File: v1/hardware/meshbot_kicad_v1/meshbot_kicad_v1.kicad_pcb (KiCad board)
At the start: 2 copper layers, 51.9 x 23.2 mm, 9 parts, among them J1 Conn_01x02_Socket, J2 Conn_01x04_Pin, J3 Conn_01x04_Pin, J4 Conn_01x01_Socket, SW1 SW_Push, U1 wio-sx1262, U2 nice_nano_clean

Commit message: update
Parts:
- added D2: LED, LED_THT:LED_D5.0mm, F.Cu at (29.4, 1.60)
- added H1: MountingHole, MountingHole:MountingHole_3.2mm_M3, F.Cu at (0.00, 0.00)
- added H2: MountingHole, MountingHole:MountingHole_3.2mm_M3, F.Cu at (81.0, 0.00)
- added H3: MountingHole, MountingHole:MountingHole_3.2mm_M3, F.Cu at (81.0, 66.0)
- added H4: MountingHole, MountingHole:MountingHole_3.2mm_M3, F.Cu at (0.10, 66.0)
- added J11: Conn_01x03_Pin, Connector_PinHeader_2.54mm:PinHeader_1x03_P2.54mm_Vertical, F.Cu at (24.3, 57.4)
- added J12: Conn_01x03_Pin, Connector_PinHeader_2.54mm:PinHeader_1x03_P2.54mm_Vertical, F.Cu at (24.2, 64.3)
- added J13: Conn_01x08_Socket, Connector_PinSocket_2.54mm:PinSocket_1x08_P2.54mm_Vertical, F.Cu at (5.62, 1.38)
- added J5: Conn_01x04_Pin, footprints:ssd1306_a, F.Cu at (63.0, 28.1)
- added J6: Screw_Terminal_01x04, TerminalBlock_Phoenix:TerminalBlock_Phoenix_MKDS-1,5-4-5.08_1x04_P5.08mm_Horizontal, F.Cu at (45.7, 62.3)
- added J7: Screw_Terminal_01x03, TerminalBlock_Phoenix:TerminalBlock_Phoenix_MKDS-1,5-3-5.08_1x03_P5.08mm_Horizontal, F.Cu at (29.4, 62.3)
- added J8: Conn_01x03_Socket, footprints:usual_switch, F.Cu at (73.2, 1.70)
- added J9: Conn_01x02_Socket, Buzzer_Beeper:Buzzer_12x9.5RM7.6, F.Cu at (36.8, 19.7)
- added R3: R, Resistor_THT:R_Axial_DIN0204_L3.6mm_D1.6mm_P1.90mm_Vertical, F.Cu at (24.8, 4.30)
- added R4: R, Resistor_THT:R_Axial_DIN0204_L3.6mm_D1.6mm_P1.90mm_Vertical, F.Cu at (18.2, 4.30)
- added R5: R, Resistor_THT:R_Axial_DIN0204_L3.6mm_D1.6mm_P1.90mm_Vertical, F.Cu at (54.0, 3.00)
- added R6: R, Resistor_THT:R_Axial_DIN0204_L3.6mm_D1.6mm_P1.90mm_Vertical, F.Cu at (51.5, 3.00)
- added R7: R, Resistor_THT:R_Axial_DIN0204_L3.6mm_D1.6mm_P1.90mm_Vertical, F.Cu at (49.0, 3.00)
- added SW2: SW_Push, Button_Switch_THT:SW_Tactile_SPST_Angled_PTS645Vx31-2LFS, F.Cu at (-0.10, 40.6)
- added SW3: SW_Push, Button_Switch_THT:SW_Tactile_SPST_Angled_PTS645Vx31-2LFS, F.Cu at (81.5, 26.5)
- added SW4: SW_Push, Button_Switch_THT:SW_Tactile_SPST_Angled_PTS645Vx31-2LFS, F.Cu at (81.5, 36.1)
- added SW5: SW_Push, Button_Switch_THT:SW_Tactile_SPST_Angled_PTS645Vx31-2LFS, F.Cu at (81.5, 45.7)
- added SW6: SW_Push, Button_Switch_THT:SW_Tactile_SPST_Angled_PTS645Vx31-2LFS, F.Cu at (81.5, 55.4)
- added SW7: SW_Push, Button_Switch_THT:SW_Tactile_SPST_Angled_PTS645Vx31-2LFS, F.Cu at (-0.10, 50.2)
- added SW8: SW_Push, Button_Switch_THT:SW_Tactile_SPST_Angled_PTS645Vx31-2LFS, F.Cu at (-0.10, 59.8)
- added U3: nice_nano_clean, footprints:nice_nano_cleanest, F.Cu at (65.5, 14.6)
- added U4: grove_a, footprints:grove_a, F.Cu at (14.5, 59.9)
- added U5: grove_a, footprints:grove_rightangle, F.Cu at (73.1, 60.0)
- J2: footprint Connector_PinHeader_2.54mm:PinHeader_1x04_P2.54mm_Vertical -> footprints:gps_ublox_blue
- J3: footprint Connector_PinHeader_2.54mm:PinHeader_1x04_P2.54mm_Vertical -> footprints:ssd1306_a
- SW1: footprint Button_Switch_THT:SW_PUSH_6mm -> Button_Switch_THT:SW_Tactile_SPST_Angled_PTS645Vx31-2LFS
- moved SW1 96.7 mm to (-0.10, 31.0)
- moved J4 79.4 mm to (41.4, -1.20)
- moved U2 66.1 mm to (15.7, 14.7)
- moved U1 64.6 mm to (34.8, 12.2), turned to 0 degrees
- moved R2 60.4 mm to (5.60, 4.30), turned to 180 degrees
- moved R1 59.8 mm to (11.7, 4.30), turned to 180 degrees
- moved J3 58.5 mm to (26.1, 28.1), turned to -90 degrees
- moved J1 52.8 mm to (60.8, 2.40), turned to 180 degrees
- moved J2 45.4 mm to (37.0, 37.8), turned to -90 degrees
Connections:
- net BATT_MEASURE renamed MESH_BATT_MEASURE
- net MICRO_RST renamed MESH_RST
- net SCL renamed SCL_MESH
- net SDA renamed SDA_MESH
- J1 pad 1: BAT -> V_EXT
- J3 pad 1: GND -> 3V3
- J3 pad 2: 3V3 -> GND
- U2 pad 1: unconnected-(U2-TX0/P0.06-Pad1) -> MESH_TX
- U2 pad 12: unconnected-(U2-P1.06-Pad12) -> MESH_BUTTON_C
- U2 pad 2: unconnected-(U2-RX1/P0.08-Pad2) -> MESH_RX
- U2 pad 8: unconnected-(U2-P0.24-Pad8) -> MESH_BUTTON_A
- U2 pad 9: unconnected-(U2-P1.00-Pad9) -> MESH_BUTTON_B
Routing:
- net GND: track 111.4 -> 0.00 mm, vias 11 -> 0
- net GPS_TX: track 70.5 -> 0.00 mm, vias 4 -> 0
- net 3V3: track 62.9 -> 0.00 mm, vias 5 -> 0
- net GPS_RX: track 60.5 -> 0.00 mm, vias 5 -> 0
- net BAT: track 59.6 -> 0.00 mm, vias 3 -> 0
- net BUSY: track 37.5 -> 0.00 mm, vias 4 -> 0
- net SDA_MESH: track 36.6 -> 0.00 mm, vias 3 -> 0
- net MESH_RST: track 36.5 -> 0.00 mm, vias 1 -> 0
- net RF_SW: track 32.5 -> 0.00 mm, vias 2 -> 0
- net SCL_MESH: track 31.4 -> 0.00 mm, vias 3 -> 0
- net MOSI: track 24.0 -> 0.00 mm, vias 2 -> 0
- net MISO: track 23.5 -> 0.00 mm, vias 2 -> 0
- net DIO1: track 23.1 -> 0.00 mm, vias 4 -> 0
- net CS: track 22.8 -> 0.00 mm, vias 2 -> 0
- net SCK: track 18.3 -> 0.00 mm, vias 2 -> 0
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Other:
- board size 51.9 x 23.2 mm -> 88 x 72.7 mm
- board text added: "+"
- board text added: "-"
- board text added: "1W"
- board text added: "2"
- board text added: "29"
- board text added: "3V3"
- board text added: "A"
- board text added: "ANT"
- board text added: "B"
- board text added: "Buzzer"
- board text added: "C"
- board text added: "GPS_RX"
- board text added: "GPS_TX"
- board text added: "M:A"
- board text added: "M:B"
- board text added: "M:C"
- board text added: "M:RST"
- board text added: "M:SCL"
- board text added: "M:SDA"
- board text added: "MESHBOT VER 1"
- board text added: "OFF"
- board text added: "ON"
- board text added: "RX"
- board text added: "SSD1306"
- board text added: "S_A"
- board text added: "S_B"
- board text added: "TX"
- board text added: "VEX"
- board text added: "edgecollective.io/meshbot"
- board text added: "v1"
- board text removed: "20"
- board text removed: "22"
- board text removed: "ANTENNA"
- board text removed: "v0.2"
- board text removed: "waterbearfieldschool.org/thistle"

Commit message: update
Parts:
- D2: footprint LED_THT:LED_D5.0mm -> LED_THT:LED_D3.0mm
- moved J8 59.1 mm to (14.1, -0.10)
- moved J13 52.0 mm to (57.6, 2.27)
- moved J1 35.3 mm to (25.6, 0.40)
- moved D2 3.10 mm to (32.3, 0.50)
- moved R2 2.01 mm to (3.60, 4.20), turned to 0 degrees
- moved R1 2.01 mm to (9.70, 4.20), turned to 0 degrees
- moved R3 0.41 mm to (24.4, 4.20)
- moved R4 0.32 mm to (17.9, 4.20)
- moved J12 0.20 mm to (24.2, 64.5)
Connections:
- J13 pad 4: GND -> SDA
- J13 pad 6: SDA -> P0.2
- J13 pad 7: P0.2 -> P0.29
- J13 pad 8: P0.29 -> GND
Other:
- board text added: "NEO6M GPS"
- board text added: "S:A"
- board text added: "S:B"
- board text added: "VEXT"
- board text removed: "S_A"
- board text removed: "S_B"
- board text removed: "VEX"

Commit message: update
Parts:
- moved H1 112.7 mm to (104.4, 42.5)
- moved H2 112.7 mm to (185.4, 42.5)
- moved H3 112.7 mm to (185.4, 108.5)
- moved H4 112.7 mm to (104.5, 108.5)
- moved J1 112.7 mm to (130.0, 42.9)
- moved J11 112.7 mm to (128.7, 99.9)
- moved J12 112.7 mm to (128.6, 107.0)
- moved J13 112.7 mm to (162.0, 44.8)
- moved J2 112.7 mm to (141.4, 80.3)
- moved J3 112.7 mm to (130.5, 70.6)
- moved J4 112.7 mm to (145.8, 41.3)
- moved J7 112.7 mm to (133.8, 104.8)
- moved J8 112.7 mm to (118.5, 42.4)
- moved R1 112.7 mm to (114.1, 46.7)
- moved R2 112.7 mm to (108.0, 46.7)
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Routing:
- net BAT: track 0.00 -> 143.1 mm, vias 0 -> 13
- net GND: track 0.00 -> 74.3 mm, vias 0 -> 12
- net V_EXT: track 0.00 -> 54.9 mm, vias 0 -> 3
- net 3V3: track 0.00 -> 42.4 mm, vias 0 -> 2

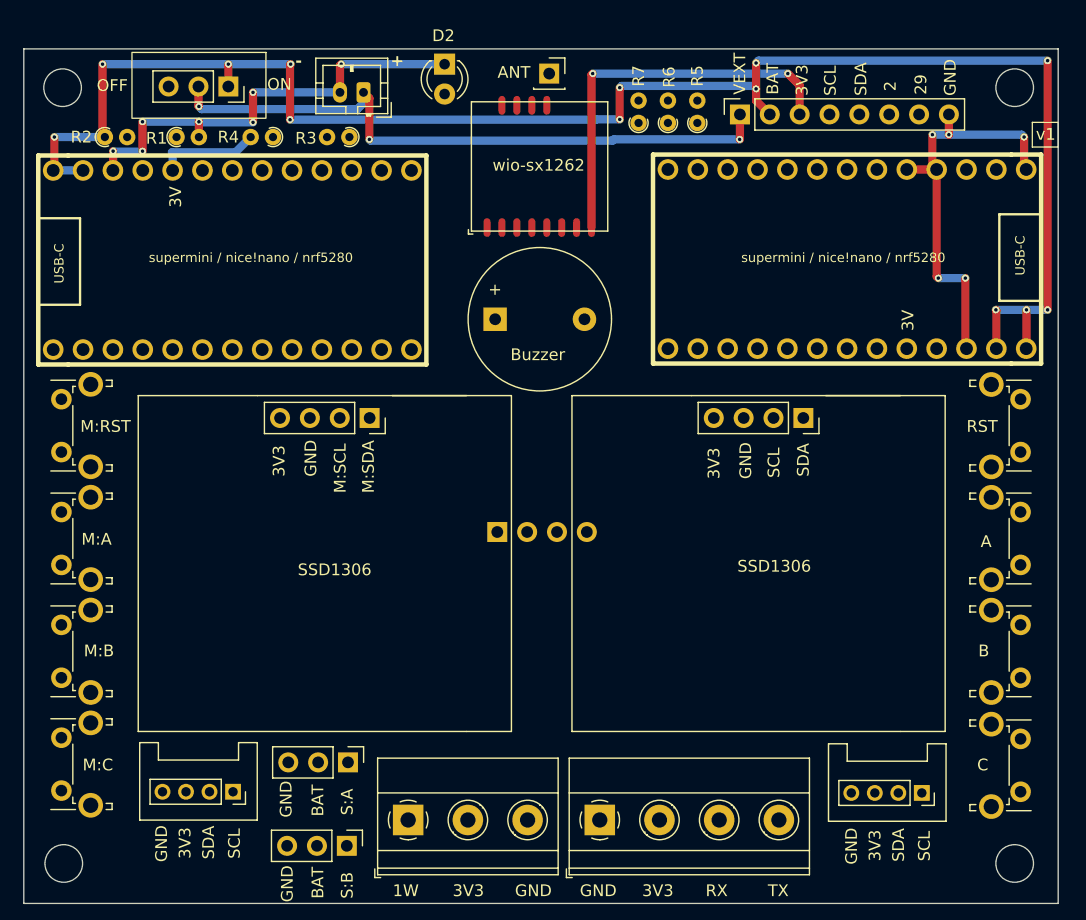
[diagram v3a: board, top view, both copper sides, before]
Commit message: routed power
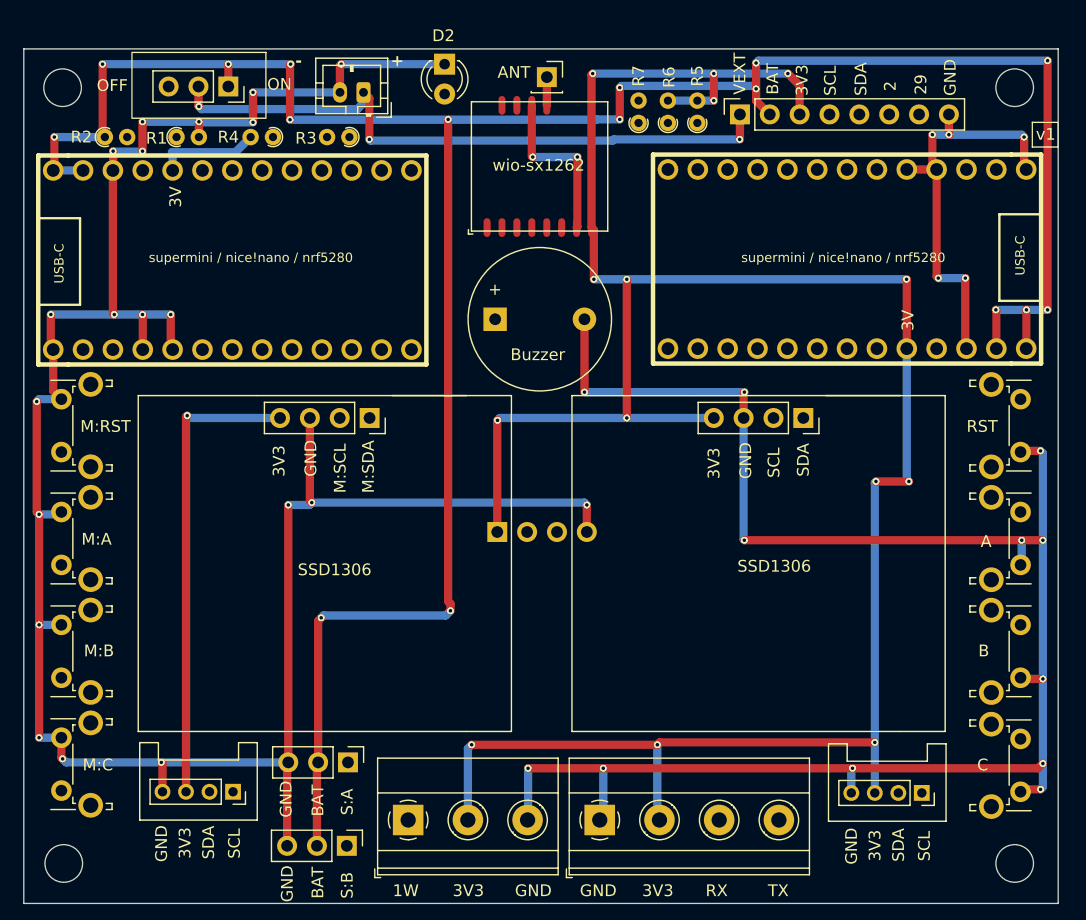
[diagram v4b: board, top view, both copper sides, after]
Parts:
- moved J4 0.36 mm to (145.6, 41.6)
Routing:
- net GND: track 74.3 -> 398.8 mm, vias 12 -> 39
- net 3V3: track 42.4 -> 253.5 mm, vias 2 -> 15
- net BAT: track 143.1 -> 215.8 mm, vias 13 -> 16
- net ANT: track 0.00 -> 2.40 mm

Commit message: update
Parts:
- moved D2 0.91 mm to (136.4, 41.3)
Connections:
- U4 pad 3: SDA -> SDA_MESH
- U4 pad 4: SCL -> SCL_MESH
- U5 pad 3: SDA_MESH -> SDA
- U5 pad 4: SCL_MESH -> SCL
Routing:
- net SERVO_B: track 0.00 -> 108.0 mm, vias 0 -> 5
- net SCL: track 0.00 -> 106.4 mm, vias 0 -> 8
- net 1WIRE: track 0.00 -> 93.7 mm, vias 0 -> 4
- net MESH_RX: track 0.00 -> 92.8 mm, vias 0 -> 4
- net UART_RX: track 0.00 -> 90.2 mm, vias 0 -> 4
- net MESH_TX: track 0.00 -> 88.7 mm, vias 0 -> 3
- net SERVO_A: track 0.00 -> 85.4 mm, vias 0 -> 4
- net SDA: track 0.00 -> 84.6 mm, vias 0 -> 5
- net SDA_MESH: track 0.00 -> 80.5 mm, vias 0 -> 4
- net 3V3: track 253.5 -> 322.6 mm, vias 15 -> 21
- net MESH_BUTTON_C: track 0.00 -> 66.0 mm, vias 0 -> 3
- net SCL_MESH: track 0.00 -> 64.8 mm, vias 0 -> 2
- net MESH_BUTTON_A: track 0.00 -> 64.3 mm, vias 0 -> 3
- net UART_TX: track 0.00 -> 62.6 mm, vias 0 -> 2
- net BUTTON_A: track 0.00 -> 58.4 mm, vias 0 -> 1
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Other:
- board text added: "MESHBOT version 1"
- board text added: "waterbearfieldschool.org/meshbot"
- board text removed: "MESHBOT VER 1"
- board text removed: "edgecollective.io/meshbot"
